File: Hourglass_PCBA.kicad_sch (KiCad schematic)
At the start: 0 parts

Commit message: Progress commit. Added MCU + IMU.
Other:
- added sheet LSM6DSOX 6-Axis IMU (IMU.kicad_sch)
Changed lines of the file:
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@@
+		)
+	)
+	(sheet
+		(at 121.92 87.63)
+		(size 41.91 26.67)
+		(fields_autoplaced yes)
+		(stroke
+			(width 0.1524)
+			(type solid)
+		)
+		(fill
+			(color 0 0 0 0.0000)
+		)
+		(property "Sheetname" "LSM6DSOX 6-Axis IMU"
+			(at 121.92 86.9184 0)
+			(effects
+				(font
+					(size 1.27 1.27)
+				)
+				(justify left bottom)
+			)
+		)
+		(property "Sheetfile" "IMU.kicad_sch"
+			(at 121.92 114.8846 0)
+			(effects
+				(font
+					(size 1.27 1.27)
+				)
+				(justify left top)
+			)
+		)
+		(instances
+			(project "Hourglass_PCBA"
+				(path "/a75630d2-15a7-42bc-8ce0-7846cbd1da6b"
+					(page "6")
+				)
+			)
 		)
 	)

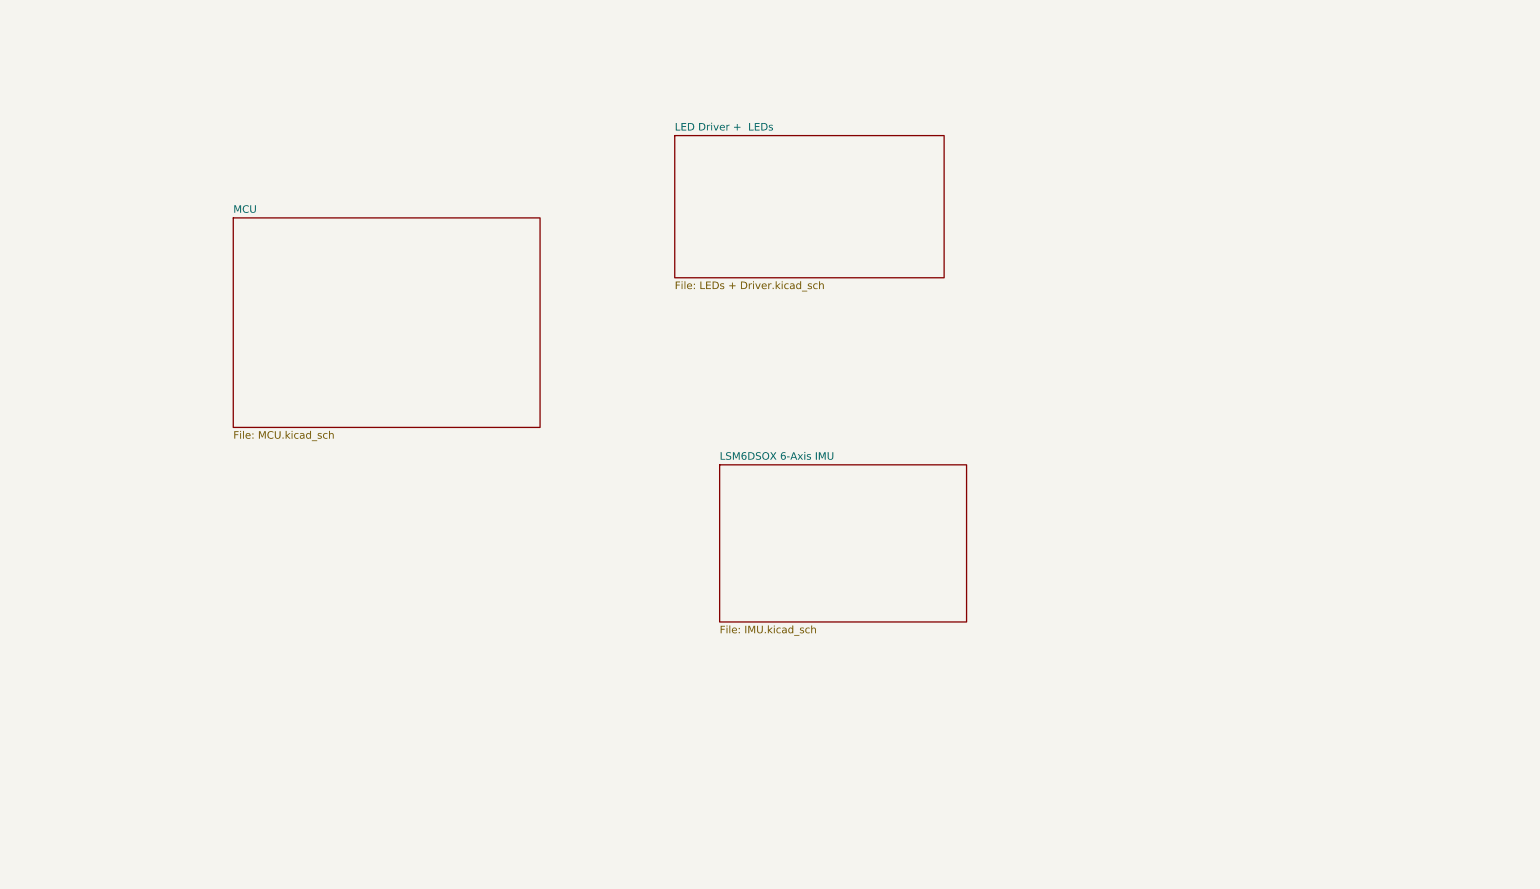
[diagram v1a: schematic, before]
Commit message: Finished power section.
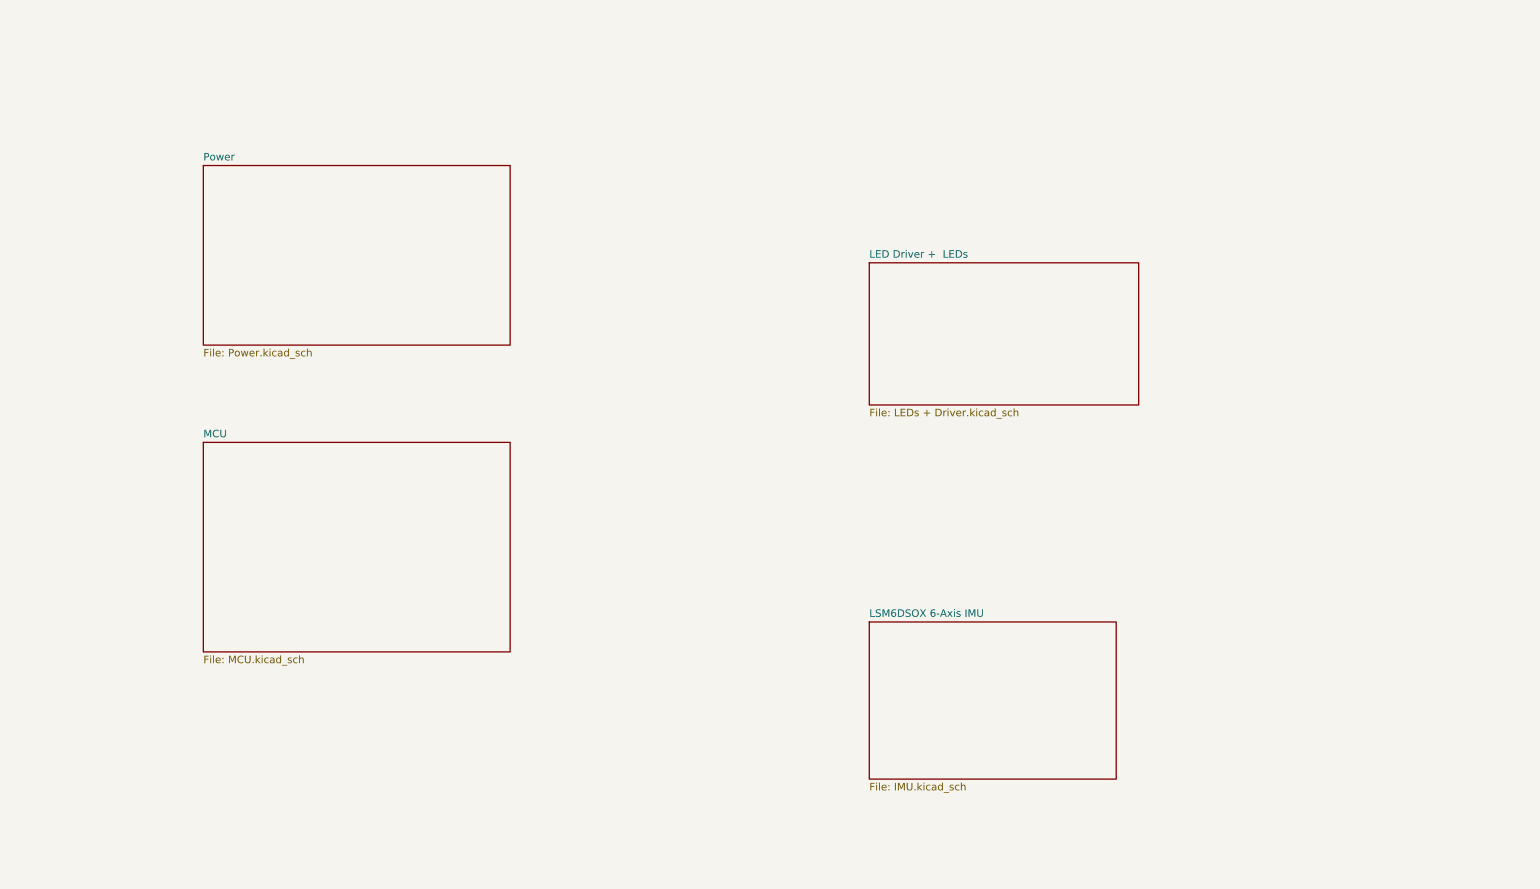
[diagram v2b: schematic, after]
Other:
- added sheet Power (Power.kicad_sch)
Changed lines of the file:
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@@
 (kicad_sch
-	(version 20231120)
+	(version 20250114)
 	(generator "eeschema")
-	(generator_version "8.0")
+	(generator_version "9.0")
 	(paper "A")
 	(title_block
@@
 	)
 	(sheet
-		(at 114.3 31.75)
+		(at 147.32 53.34)
 		(size 45.72 24.13)
+		(exclude_from_sim no)
+		(in_bom yes)
+		(on_board yes)
+		(dnp no)
 		(fields_autoplaced yes)
 		(stroke
@@
 		)
 		(property "Sheetname" "LED Driver +  LEDs"
-			(at 114.3 31.0384 0)
+			(at 147.32 52.6284 0)
 			(effects
 				(font
@@
 		)
 		(property "Sheetfile" "LEDs + Driver.kicad_sch"
-			(at 114.3 56.4646 0)
+			(at 147.32 78.0546 0)
 			(effects
 				(font
@@
 	)
 	(sheet
-		(at 39.37 45.72)
+		(at 34.29 36.83)
+		(size 52.07 30.48)
+		(exclude_from_sim no)
+		(in_bom yes)
+		(on_board yes)
+		(dnp no)
+		(fields_autoplaced yes)
+		(stroke
+			(width 0.1524)
+			(type solid)
+		)
+		(fill
+			(color 0 0 0 0.0000)
+		)
+		(property "Sheetname" "Power"
+			(at 34.29 36.1184 0)
+			(effects
+				(font
+					(size 1.27 1.27)
+				)
+				(justify left bottom)
+			)
+		)
+		(property "Sheetfile" "Power.kicad_sch"
+			(at 34.29 67.8946 0)
+			(effects
+				(font
+					(size 1.27 1.27)
+				)
+				(justify left top)
+			)
+		)
+		(instances
+			(project "Hourglass_PCBA"
+				(path "/a75630d2-15a7-42bc-8ce0-7846cbd1da6b"
+					(page "7")
+				)
+			)
+		)
+	)
+	(sheet
+		(at 34.29 83.82)
 		(size 52.07 35.56)
+		(exclude_from_sim no)
+		(in_bom yes)
+		(on_board yes)
+		(dnp no)
 		(fields_autoplaced yes)
 		(stroke
@@
 		)
 		(property "Sheetname" "MCU"
-			(at 39.37 45.0084 0)
+			(at 34.29 83.1084 0)
 			(effects
 				(font
@@
 		)
 		(property "Sheetfile" "MCU.kicad_sch"
-			(at 39.37 81.8646 0)
+			(at 34.29 119.9646 0)
 			(effects
 				(font
@@
 	)
 	(sheet
-		(at 121.92 87.63)
+		(at 147.32 114.3)
 		(size 41.91 26.67)
+		(exclude_from_sim no)
+		(in_bom yes)
+		(on_board yes)
+		(dnp no)
 		(fields_autoplaced yes)
 		(stroke
@@
 		)
 		(property "Sheetname" "LSM6DSOX 6-Axis IMU"
-			(at 121.92 86.9184 0)
+			(at 147.32 113.5884 0)
 			(effects
 				(font
@@
 		)
 		(property "Sheetfile" "IMU.kicad_sch"
-			(at 121.92 114.8846 0)
+			(at 147.32 141.5546 0)
 			(effects
 				(font
@@
 		)
 	)
+	(embedded_fonts no)
 )

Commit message: Finished LSM6DSOX schematic
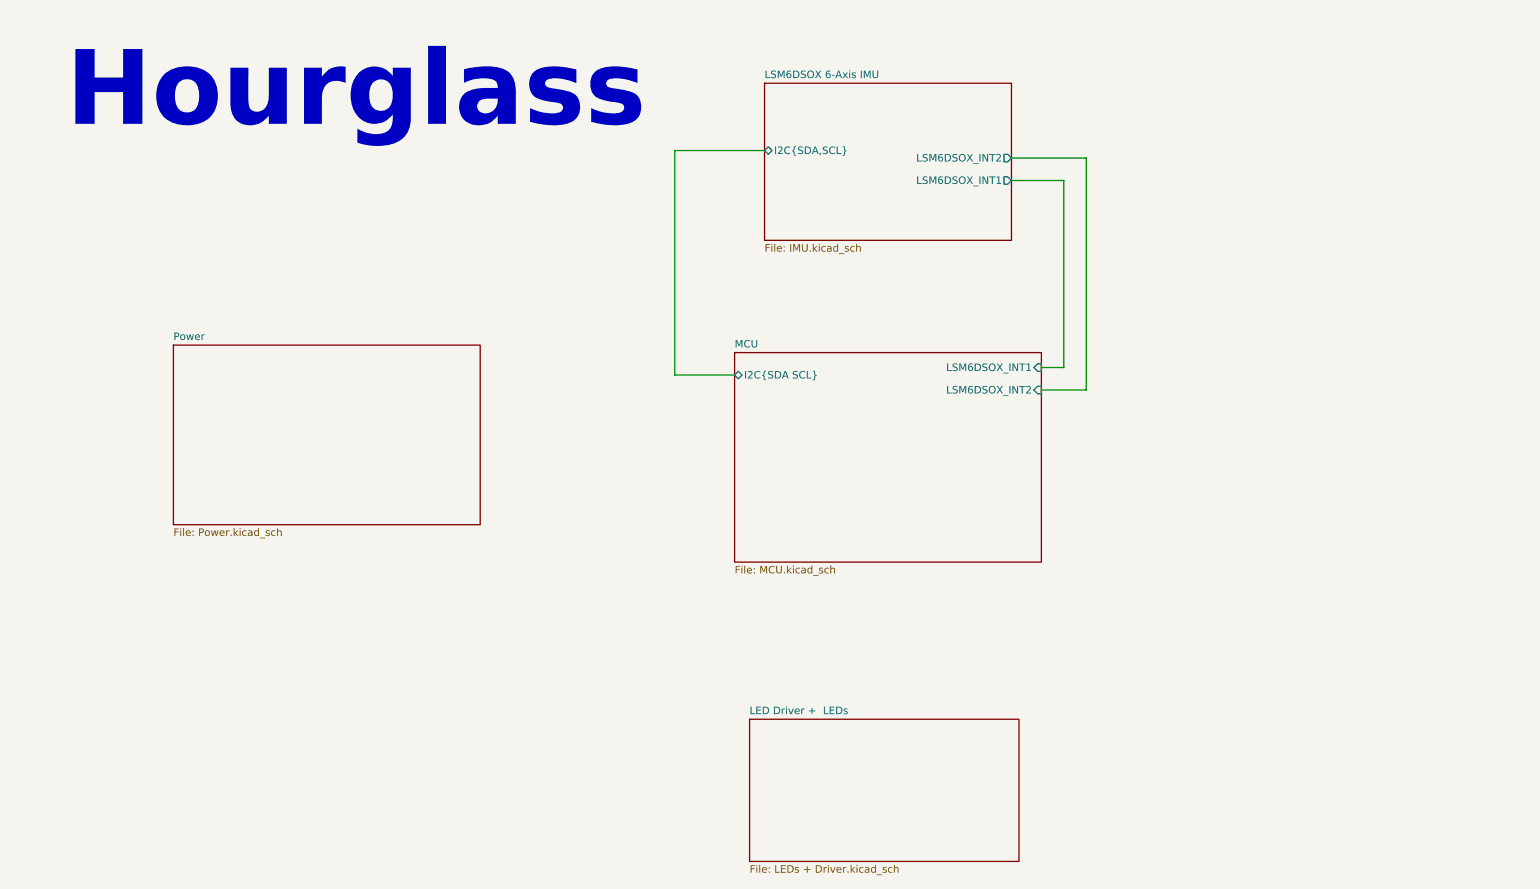
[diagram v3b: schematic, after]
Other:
- sheet LSM6DSOX 6-Axis IMU ports: added I2C{SDA,SCL}, LSM6DSOX_INT1, LSM6DSOX_INT2; removed none
- sheet MCU ports: added I2C{SDA SCL}, LSM6DSOX_INT1, LSM6DSOX_INT2; removed none
- note added: "Hourglass"
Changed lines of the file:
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@@
 		(rev "01")
 	)
+	(text "Hourglass"
+		(exclude_from_sim yes)
+		(at 60.198 24.13 0)
+		(effects
+			(font
+				(face "KiCad Font")
+				(size 12.7 12.7)
+				(thickness 0.254)
+				(bold yes)
+			)
+		)
+	)
+	(wire
+		(pts
+			(xy 184.15 35.56) (xy 184.15 74.93)
+		)
+		(stroke
+			(width 0)
+			(type default)
+		)
+	)
+	(wire
+		(pts
+			(xy 180.34 39.37) (xy 180.34 71.12)
+		)
+		(stroke
+			(width 0)
+			(type default)
+		)
+	)
+	(wire
+		(pts
+			(xy 124.46 72.39) (xy 114.3 72.39)
+		)
+		(stroke
+			(width 0)
+			(type default)
+		)
+	)
+	(wire
+		(pts
+			(xy 171.45 39.37) (xy 180.34 39.37)
+		)
+		(stroke
+			(width 0)
+			(type default)
+		)
+	)
+	(wire
+		(pts
+			(xy 114.3 72.39) (xy 114.3 34.29)
+		)
+		(stroke
+			(width 0)
+			(type default)
+		)
+	)
+	(wire
+		(pts
+			(xy 184.15 74.93) (xy 176.53 74.93)
+		)
+		(stroke
+			(width 0)
+			(type default)
+		)
+	)
+	(wire
+		(pts
+			(xy 171.45 35.56) (xy 184.15 35.56)
+		)
+		(stroke
+			(width 0)
+			(type default)
+		)
+	)
+	(wire
+		(pts
+			(xy 180.34 71.12) (xy 176.53 71.12)
+		)
+		(stroke
+			(width 0)
+			(type default)
+		)
+	)
+	(wire
+		(pts
+			(xy 114.3 34.29) (xy 129.54 34.29)
+		)
+		(stroke
+			(width 0)
+			(type default)
+		)
+	)
 	(sheet
-		(at 147.32 53.34)
+		(at 127 130.81)
 		(size 45.72 24.13)
 		(exclude_from_sim no)
@@
 		)
 		(fill
-			(color 0 0 0 0.0000)
+			(color 0 132 0 1.0000)
 		)
 		(property "Sheetname" "LED Driver +  LEDs"
-			(at 147.32 52.6284 0)
+			(at 127 130.0984 0)
 			(effects
 				(font
@@
 		)
 		(property "Sheetfile" "LEDs + Driver.kicad_sch"
-			(at 147.32 78.0546 0)
+			(at 127 155.5246 0)
 			(effects
 				(font
@@
 	)
 	(sheet
-		(at 34.29 36.83)
+		(at 29.21 67.31)
 		(size 52.07 30.48)
 		(exclude_from_sim no)
@@
 		)
 		(fill
-			(color 0 0 0 0.0000)
+			(color 0 132 0 1.0000)
 		)
 		(property "Sheetname" "Power"
-			(at 34.29 36.1184 0)
+			(at 29.21 66.5984 0)
 			(effects
 				(font
@@
 		)
 		(property "Sheetfile" "Power.kicad_sch"
-			(at 34.29 67.8946 0)
+			(at 29.21 98.3746 0)
 			(effects
 				(font
@@
 	)
 	(sheet
-		(at 34.29 83.82)
+		(at 124.46 68.58)
 		(size 52.07 35.56)
 		(exclude_from_sim no)
@@
 		)
 		(fill
-			(color 0 0 0 0.0000)
+			(color 0 132 0 1.0000)
 		)
 		(property "Sheetname" "MCU"
-			(at 34.29 83.1084 0)
+			(at 124.46 67.8684 0)
 			(effects
 				(font
@@
 		)
 		(property "Sheetfile" "MCU.kicad_sch"
-			(at 34.29 119.9646 0)
+			(at 124.46 104.7246 0)
 			(effects
 				(font
@@
 				)
 				(justify left top)
+			)
+		)
+		(pin "I2C{SDA SCL}" bidirectional
+			(at 124.46 72.39 180)
+			(effects
+				(font
+					(size 1.27 1.27)
+				)
+				(justify left)
+			)
+		)
+		(pin "LSM6DSOX_INT2" input
+			(at 176.53 74.93 0)
+			(effects
+				(font
+					(size 1.27 1.27)
+				)
+				(justify right)
+			)
+		)
+		(pin "LSM6DSOX_INT1" input
+			(at 176.53 71.12 0)
+			(effects
+				(font
+					(size 1.27 1.27)
+				)
+				(justify right)
 			)
 		)
@@
 	)
 	(sheet
-		(at 147.32 114.3)
+		(at 129.54 22.86)
 		(size 41.91 26.67)
 		(exclude_from_sim no)
@@
 		)
 		(fill
-			(color 0 0 0 0.0000)
+			(color 0 132 0 1.0000)
 		)
 		(property "Sheetname" "LSM6DSOX 6-Axis IMU"
-			(at 147.32 113.5884 0)
+			(at 129.54 22.1484 0)
 			(effects
 				(font
@@
 		)
 		(property "Sheetfile" "IMU.kicad_sch"
-			(at 147.32 141.5546 0)
+			(at 129.54 50.1146 0)
 			(effects
 				(font
@@
 			)
 		)
+		(pin "I2C{SDA,SCL}" bidirectional
+			(at 129.54 34.29 180)
+			(effects
+				(font
+					(size 1.27 1.27)
+				)
+				(justify left)
+			)
+		)
+		(pin "LSM6DSOX_INT2" output
+			(at 171.45 35.56 0)
+			(effects
+				(font
+					(size 1.27 1.27)
+				)
+				(justify right)
+			)
+		)
+		(pin "LSM6DSOX_INT1" output
+			(at 171.45 39.37 0)
+			(effects
+				(font
+					(size 1.27 1.27)
+				)
+				(justify right)
+			)
+		)

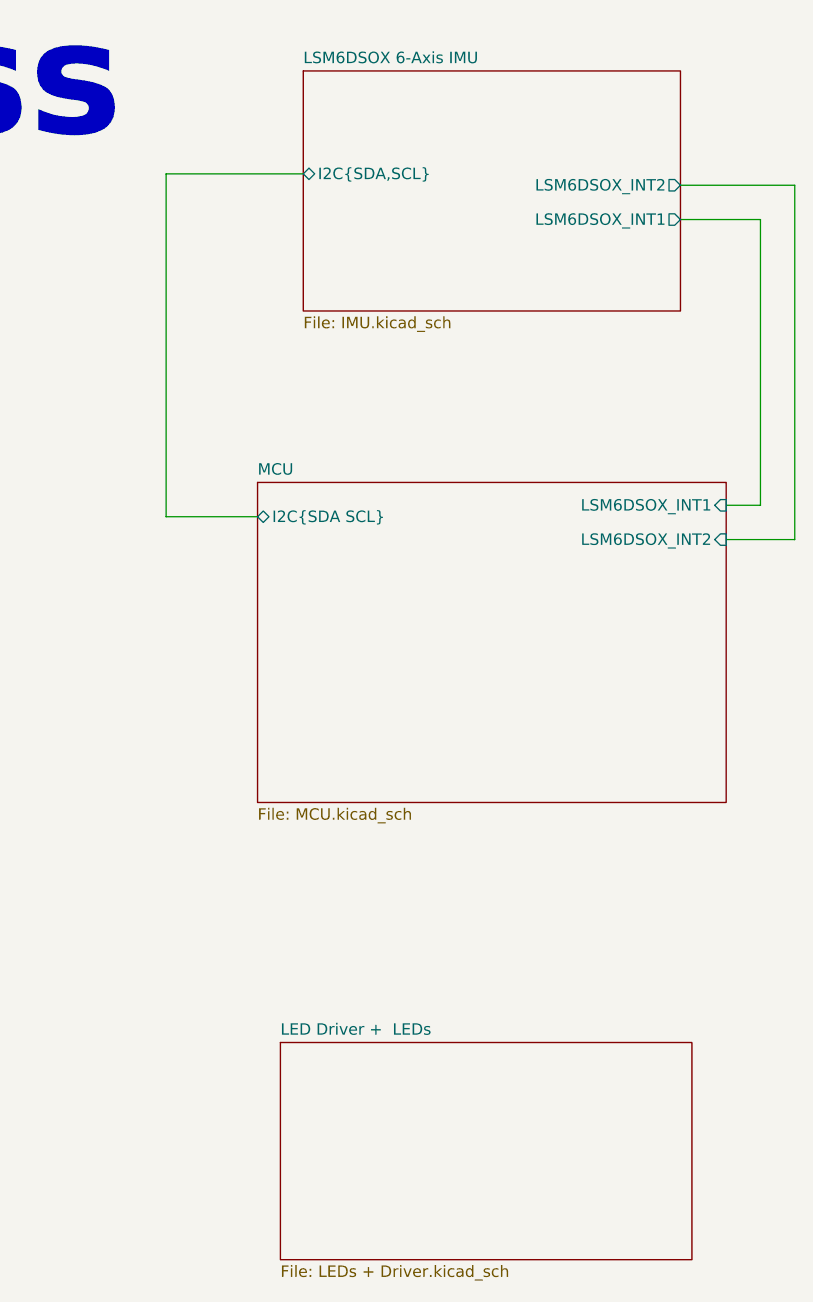
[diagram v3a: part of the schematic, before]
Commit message: Initial complete implementation of LEDS.
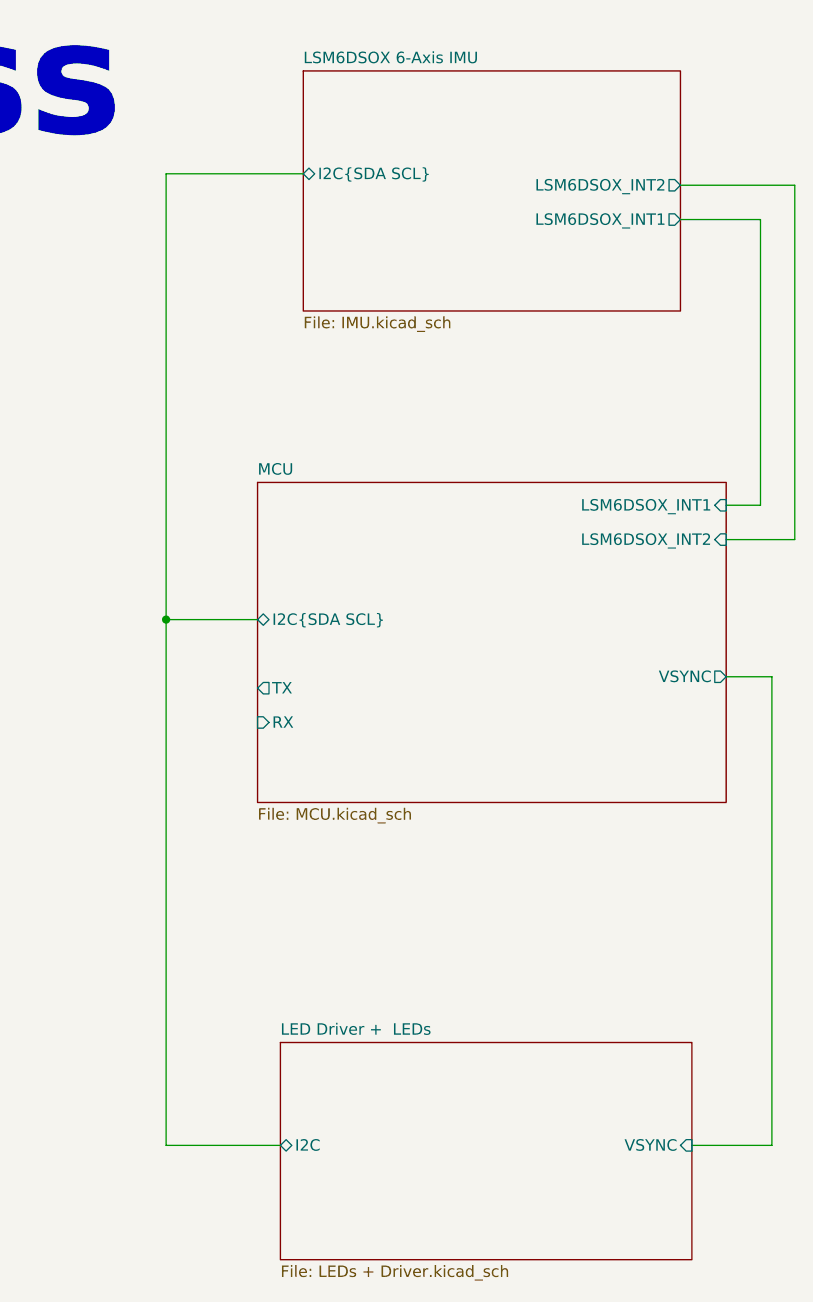
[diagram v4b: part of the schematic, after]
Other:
- sheet LED Driver +  LEDs ports: added I2C, VSYNC; removed none
- sheet LSM6DSOX 6-Axis IMU ports: added I2C{SDA SCL}; removed I2C{SDA,SCL}
- sheet MCU ports: added RX, TX, VSYNC; removed none
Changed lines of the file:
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@@
+		)
+	)
+	(junction
+		(at 114.3 83.82)
+		(diameter 0)
+		(color 0 0 0 0)
+	)
+	(wire
+		(pts
+			(xy 181.61 142.24) (xy 172.72 142.24)
+		)
+		(stroke
+			(width 0)
+			(type default)
 		)
 	)
@@
 	(wire
 		(pts
-			(xy 124.46 72.39) (xy 114.3 72.39)
+			(xy 176.53 90.17) (xy 181.61 90.17)
+		)
+		(stroke
+			(width 0)
+			(type default)
+		)
+	)
+	(wire
+		(pts
+			(xy 114.3 142.24) (xy 114.3 83.82)
+		)
+		(stroke
+			(width 0)
+			(type default)
+		)
+	)
+	(wire
+		(pts
+			(xy 124.46 83.82) (xy 114.3 83.82)
+		)
+		(stroke
+			(width 0)
+			(type default)
+		)
+	)
+	(wire
+		(pts
+			(xy 127 142.24) (xy 114.3 142.24)
 		)
 		(stroke
@@
 	(wire
 		(pts
-			(xy 114.3 72.39) (xy 114.3 34.29)
+			(xy 114.3 83.82) (xy 114.3 34.29)
 		)
 		(stroke
@@
 		(pts
 			(xy 114.3 34.29) (xy 129.54 34.29)
+		)
+		(stroke
+			(width 0)
+			(type default)
+		)
+	)
+	(wire
+		(pts
+			(xy 181.61 90.17) (xy 181.61 142.24)
 		)
 		(stroke
@@
 			)
 		)
+		(pin "VSYNC" input
+			(at 172.72 142.24 0)
+			(effects
+				(font
+					(size 1.27 1.27)
+				)
+				(justify right)
+			)
+		)
+		(pin "I2C" bidirectional
+			(at 127 142.24 180)
+			(effects
+				(font
+					(size 1.27 1.27)
+				)
+				(justify left)
+			)
+		)
 		(instances
 			(project "Hourglass_PCBA"
@@
 		)
 		(pin "I2C{SDA SCL}" bidirectional
-			(at 124.46 72.39 180)
+			(at 124.46 83.82 180)
 			(effects
 				(font
@@
 		(pin "LSM6DSOX_INT1" input
 			(at 176.53 71.12 0)
+			(effects
+				(font
+					(size 1.27 1.27)
+				)
+				(justify right)
+			)
+		)
+		(pin "RX" input
+			(at 124.46 95.25 180)
+			(effects
+				(font
+					(size 1.27 1.27)
+				)
+				(justify left)
+			)
+		)
+		(pin "TX" output
+			(at 124.46 91.44 180)
+			(effects
+				(font
+					(size 1.27 1.27)
+				)
+				(justify left)
+			)
+		)
+		(pin "VSYNC" output
+			(at 176.53 90.17 0)
 			(effects
 				(font
@@
 			)
 		)
-		(pin "I2C{SDA,SCL}" bidirectional
+		(pin "I2C{SDA SCL}" bidirectional
 			(at 129.54 34.29 180)
 			(effects
